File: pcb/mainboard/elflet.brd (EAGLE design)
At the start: 32 x 58 mm, 39 parts, among them J1 ZX62-B-5PA(33), J2 2212S-10SG-36, J3 STD-PINHD-1X6, Q1 IRLML6344TRPBF, Q2 ALS-PT19-315C/L177/TR8, SW1 SKRPACE010, U1 ESP-WROOM-32, U2 ADP3338AKCZ-3.3, U3 OSRB38C9AA, U4 BME280

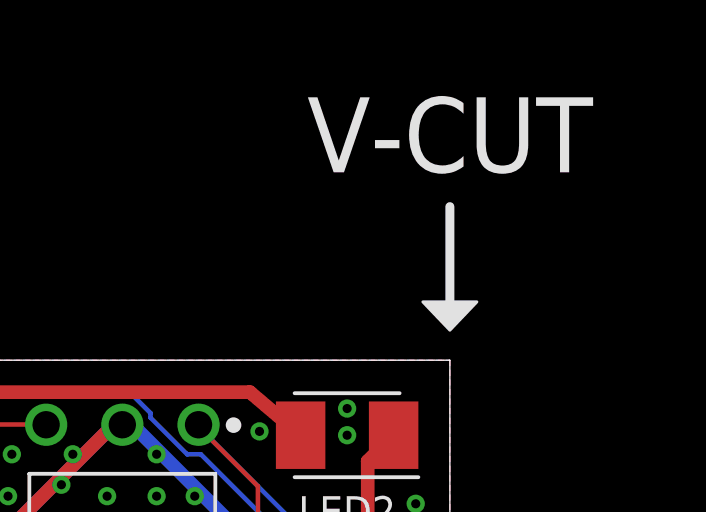
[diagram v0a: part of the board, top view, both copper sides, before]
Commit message: improve panelizing
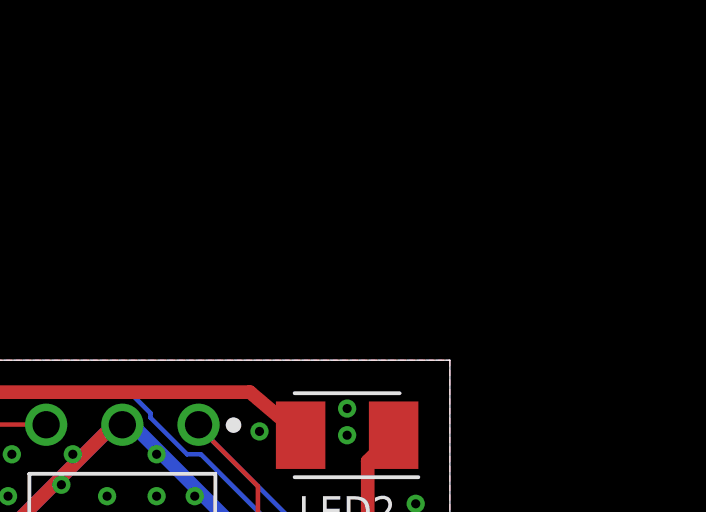
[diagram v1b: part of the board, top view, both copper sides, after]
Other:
- board text removed: "V-CUT"
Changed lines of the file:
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@@
 <rectangle x1="0" y1="0" x2="32" y2="0.7" layer="42"/>
 <dimension x1="0" y1="0" x2="32" y2="0" x3="16" y3="-7.62" textsize="1.778" layer="47" visible="yes"/>
-<polygon width="0.1" layer="21">
-<vertex x="32" y="59"/>
-<vertex x="32.9" y="59.944"/>
-<vertex x="31.1" y="59.944"/>
-</polygon>
-<wire x1="32" y1="63.119" x2="32" y2="59.563" width="0.3" layer="21"/>
-<text x="32.004" y="64.262" size="2.5" layer="21" font="vector" align="bottom-center">V-CUT</text>
 </plain>
 <attributes>

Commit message: rewiring
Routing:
- net AUX_MOSI: track 35.6 -> 64.3 mm
- net LEDB: track 31.0 -> 56.6 mm, vias 2 -> 4
- net AUX_SS: track 54.0 -> 70.6 mm, vias 1 -> 3
- net GND: track 208.0 -> 224.2 mm, vias 211 -> 165
- net TDO: track 19.7 -> 33.4 mm, vias 2 -> 4
- net TXD: track 46.7 -> 57.9 mm, vias 1 -> 3
- net +3V3: track 142.7 -> 152.1 mm, vias 4 -> 2
- net BOOT: track 80.6 -> 72.6 mm, vias 4 -> 8
- net RXD: track 44.6 -> 52.5 mm, vias 2 -> 3
- net LEDG: track 23.2 -> 31.0 mm, vias 2 -> 4
- net TDI: track 6.12 -> 13.0 mm, vias 2 -> 4
- net BUTTON: track 34.2 -> 29.7 mm
- net AUX_MISO: track 65.0 -> 60.9 mm, vias 1 -> 7
- net SDA: track 35.2 -> 38.2 mm
- net IRRX: track 42.0 -> 43.5 mm
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
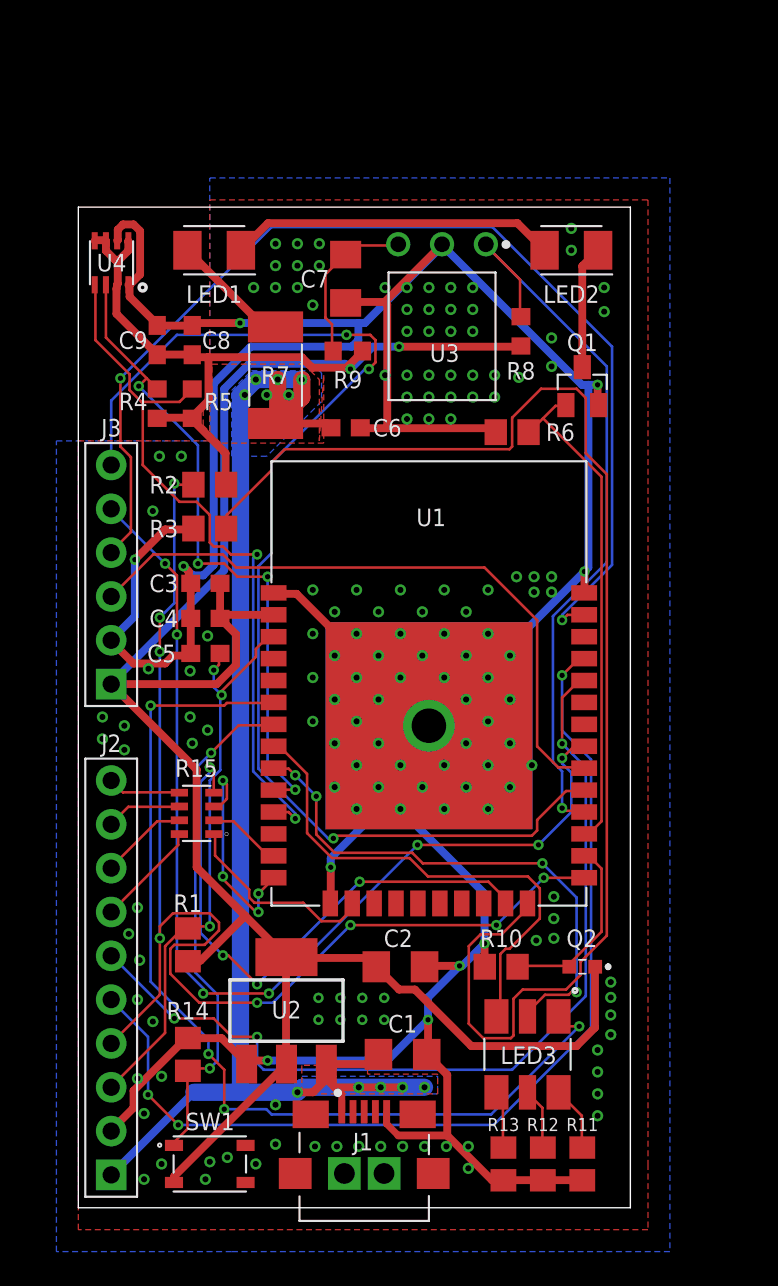
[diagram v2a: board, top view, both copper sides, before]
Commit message: fix usb connector issue
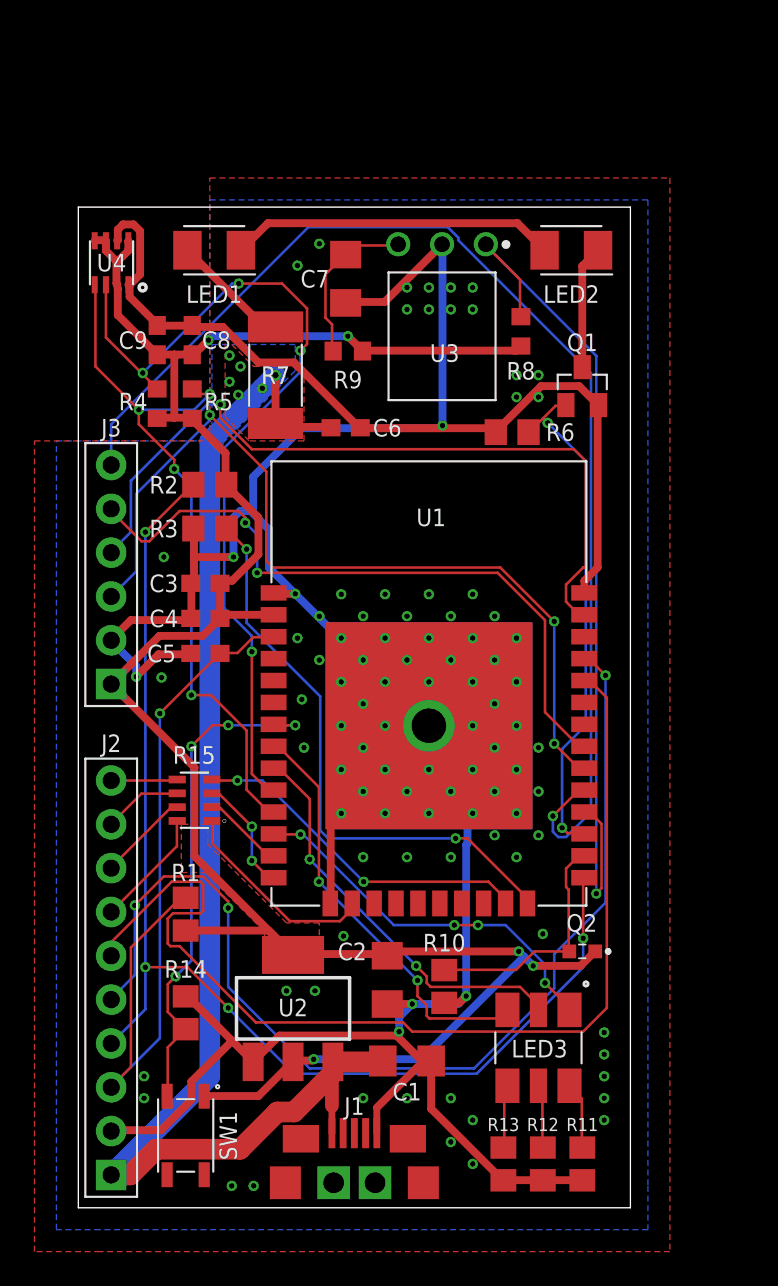
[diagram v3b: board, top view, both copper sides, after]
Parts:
- C1: value 2uF/50V(10%) -> 1uF/25V(+80-20%)
- J1: device ZX62-B-5PA(33):ZX62-B-5PA(33) -> ZX62-B-5PA(33):ZX62-B-5PA(33)-TRUE-HANDSOLD
- moved J1 4.85 mm to (16.0, 1.45)
- moved R10 3.49 mm to (21.2, 12.8), turned to 90 degrees
- moved R14 2.42 mm to (6.22, 11.3)
- moved SW1 2.16 mm to (6.22, 4.19), turned to 270 degrees
- moved R1 1.78 mm to (6.22, 17.0)
- moved C2 1.08 mm to (17.9, 13.2), turned to 270 degrees
- moved Q2 0.89 mm to (29.2, 14.9)
- moved R15 0.77 mm to (6.73, 23.6)
- moved LED3 0.74 mm to (26.7, 9.27)
- moved C1 0.46 mm to (19.1, 8.51)
- moved U2 0.40 mm to (12.4, 11.6)
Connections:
- net +3V3: now also SW1.1; no longer SW1.3
- net BUTTON: now also SW1.3; no longer SW1.1
- net LEDB: now also U1.12; no longer U1.6
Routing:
- net N$1: track 79.4 -> 33.7 mm, vias 0 -> 2
- net LEDB: track 56.6 -> 22.1 mm
- net +3V3: track 152.1 -> 130.3 mm, vias 2 -> 5
- net AUX_MISO: track 60.9 -> 39.2 mm, vias 7 -> 2
- net AUX_MOSI: track 64.3 -> 44.7 mm, vias 2 -> 1
- net GND: track 224.2 -> 206.8 mm, vias 165 -> 99
- net TDO: track 33.4 -> 20.2 mm, vias 4 -> 2
- net SDA: track 38.2 -> 50.9 mm
- net AUX_SCK: track 37.8 -> 50.2 mm, vias 0 -> 3
- net RESET: track 33.9 -> 44.2 mm, vias 3 -> 1
- net RXD: track 52.5 -> 60.7 mm, vias 3 -> 0
- net +5V: track 86.9 -> 78.7 mm, vias 12 -> 6
- net LEDG: track 31.0 -> 23.6 mm, vias 4 -> 2
- net IRRX: track 43.5 -> 50.8 mm
- net TDI: track 13.0 -> 6.78 mm, vias 4 -> 2
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- added copper zone on layer 1, net +3V3
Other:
- board text added: "ver 1.1"
- board text removed: "ver 1.0"
